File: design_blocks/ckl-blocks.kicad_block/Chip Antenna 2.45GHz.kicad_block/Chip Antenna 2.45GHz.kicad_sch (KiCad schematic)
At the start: 2 parts

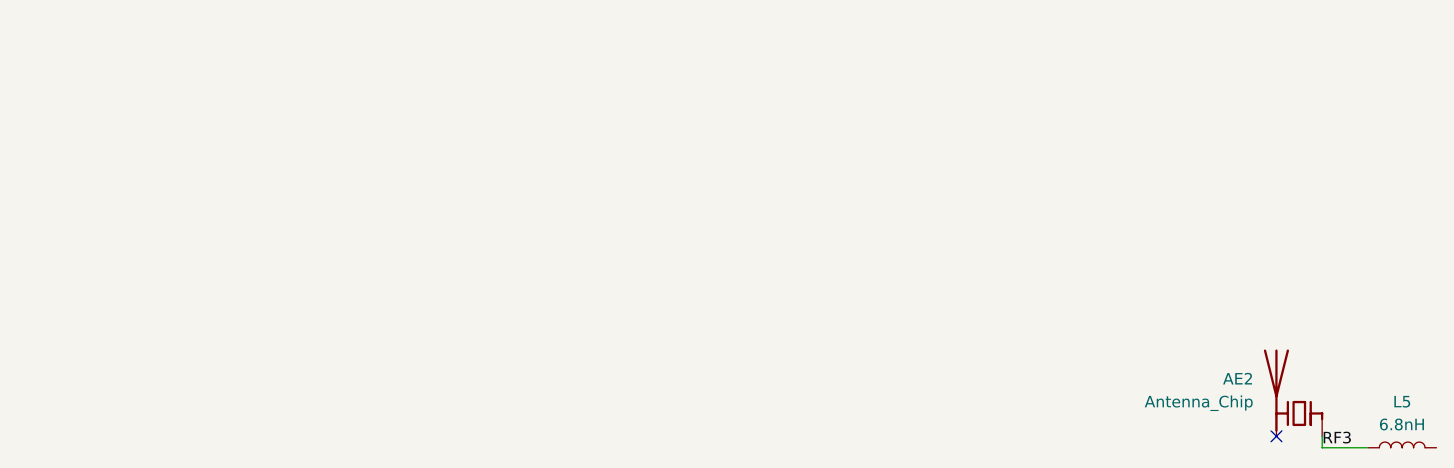
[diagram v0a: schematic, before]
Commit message: A few extra antennas
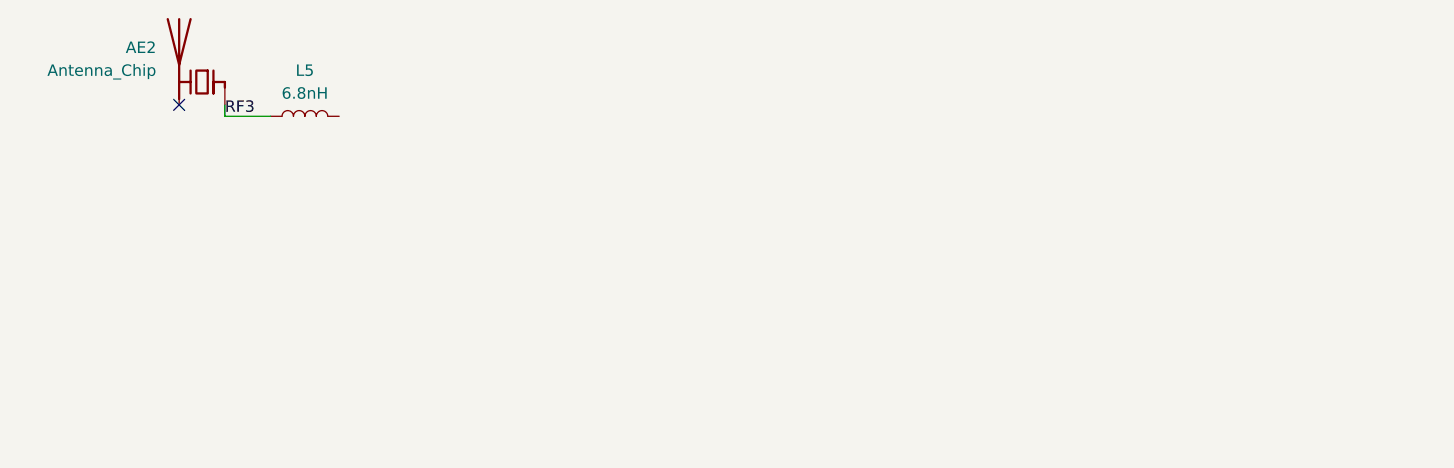
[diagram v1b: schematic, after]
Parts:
- AE2: footprint nrf52:Walsin_RFANT3216120A5T -> PCM_ckl-misc:Walsin_RFANT3216120A5T
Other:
- moved on the sheet: AE2, L5
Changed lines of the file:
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@@
 	(paper "A4")
 	(no_connect
-		(at 242.57 100.33)
+		(at 120.65 63.5)
 	)
 	(wire
 		(pts
-			(xy 247.65 100.33) (xy 247.65 101.6)
+			(xy 125.73 63.5) (xy 125.73 64.77)
 		)
 		(stroke
@@
 	(wire
 		(pts
-			(xy 247.65 101.6) (xy 252.73 101.6)
+			(xy 125.73 64.77) (xy 130.81 64.77)
 		)
 		(stroke
@@
 	)
 	(label "RF3"
-		(at 247.65 101.6 0)
+		(at 125.73 64.77 0)
 		(effects
 			(font
@@
 	(symbol
 		(lib_id "Device:Antenna_Chip")
-		(at 245.11 97.79 0)
+		(at 123.19 60.96 0)
 		(mirror y)
 		(unit 1)
@@
 		(dnp no)
 		(property "Reference" "AE2"
-			(at 240.03 93.9799 0)
+			(at 118.11 57.1499 0)
 			(show_name no)
 			(do_not_autoplace no)
@@
 		)
 		(property "Value" "Antenna_Chip"
-			(at 240.03 96.5199 0)
+			(at 118.11 59.6899 0)
 			(show_name no)
 			(do_not_autoplace no)
@@
 			)
 		)
-		(property "Footprint" "nrf52:Walsin_RFANT3216120A5T"
-			(at 247.65 93.345 0)
+		(property "Footprint" "PCM_ckl-misc:Walsin_RFANT3216120A5T"
+			(at 125.73 56.515 0)
 			(hide yes)
 			(show_name no)
@@
 		)
 		(property "Datasheet" "C127629"
-			(at 247.65 93.345 0)
+			(at 125.73 56.515 0)
 			(hide yes)
 			(show_name no)
@@
 		)
 		(property "Description" "Ceramic chip antenna with pin for PCB trace"
-			(at 245.11 97.79 0)
+			(at 123.19 60.96 0)
 			(hide yes)
 			(show_name no)
@@
 		)
 		(property "LCSC Part #" "C127629"
-			(at 245.11 97.79 0)
+			(at 123.19 60.96 0)
 			(hide yes)
 			(show_name no)
@@
 		)
 		(instances
+			(project "libmanagement"
+				(path "/3167b783-bede-465f-b0cf-2ffbbf5b7fd6"
+					(reference "AE1")
+					(unit 1)
+				)
+			)
 			(project "nrf52"
 				(path "/7c3fbfcb-953e-4e2a-9a2f-c270f824b4f7"
@@
 	(symbol
 		(lib_id "Device:L")
-		(at 256.54 101.6 90)
+		(at 134.62 64.77 90)
 		(unit 1)
 		(body_style 1)
@@
 		(dnp no)
 		(property "Reference" "L5"
-			(at 256.54 96.52 90)
+			(at 134.62 59.69 90)
 			(show_name no)
 			(do_not_autoplace no)
@@
 		)
 		(property "Value" "6.8nH"
-			(at 256.54 99.06 90)
+			(at 134.62 62.23 90)
 			(show_name no)
 			(do_not_autoplace no)
@@
 		)
 		(property "Footprint" "Inductor_SMD:L_0402_1005Metric"
-			(at 256.54 101.6 0)
+			(at 134.62 64.77 0)
 			(hide yes)
 			(show_name no)
@@
 		)
 		(property "Datasheet" ""
-			(at 256.54 101.6 0)
+			(at 134.62 64.77 0)
 			(hide yes)
 			(show_name no)
@@
 		)
 		(property "Description" "Inductor"
-			(at 256.54 101.6 0)
+			(at 134.62 64.77 0)
 			(hide yes)
 			(show_name no)
@@
 		)
 		(property "LCSC Part #" "C96056"
-			(at 256.54 101.6 90)
+			(at 134.62 64.77 90)
 			(hide yes)
 			(show_name no)
@@
 		)
 		(instances
+			(project "libmanagement"
+				(path "/3167b783-bede-465f-b0cf-2ffbbf5b7fd6"
+					(reference "L1")
+					(unit 1)
+				)
+			)
 			(project "nrf52"
 				(path "/7c3fbfcb-953e-4e2a-9a2f-c270f824b4f7"
